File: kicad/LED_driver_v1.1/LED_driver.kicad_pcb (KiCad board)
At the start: 2 copper layers, 34 x 28.2 mm, 7 parts, among them J1 Conn_01x02_Pin, J2 Conn_01x03_Pin

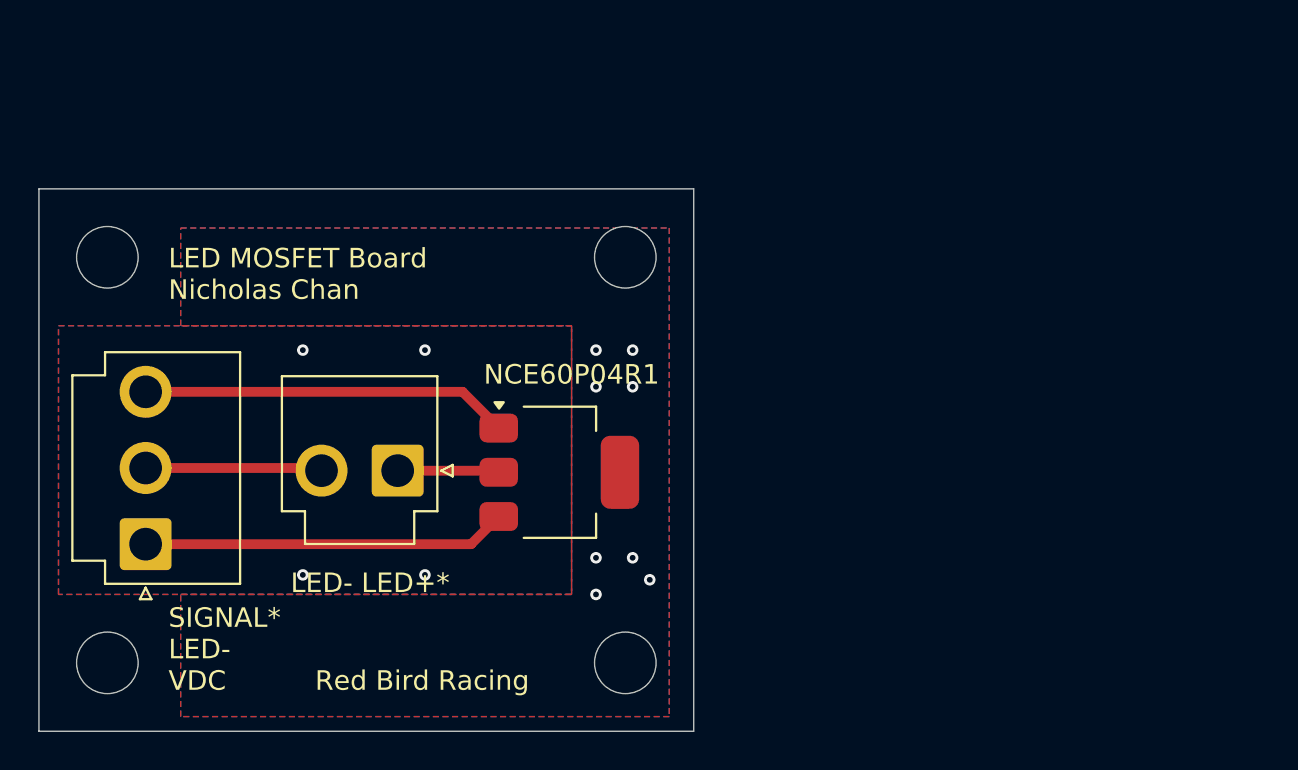
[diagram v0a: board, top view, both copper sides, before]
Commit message: LED drive v2.0
redesigned the mos cus the old one probably doesn't work
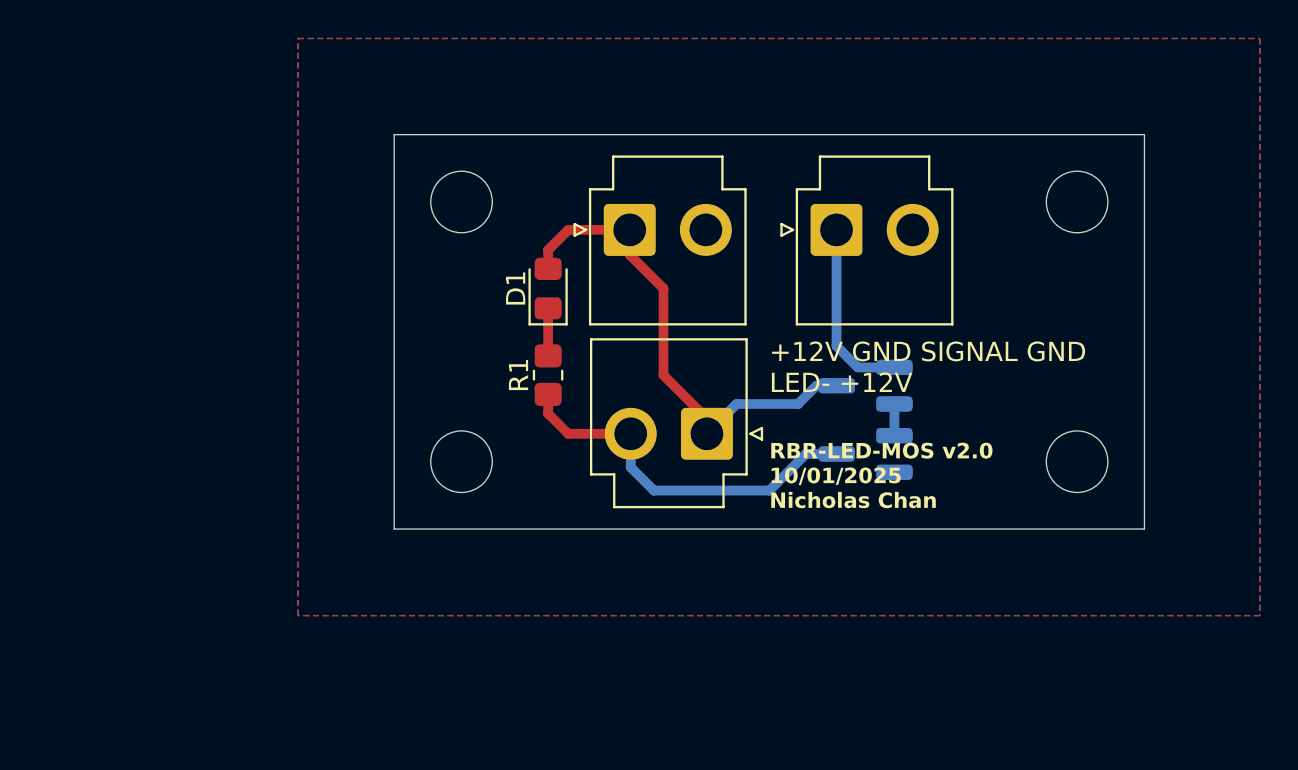
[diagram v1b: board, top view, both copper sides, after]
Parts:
- removed NCE60P04R1: NCE60P04R, Package_TO_SOT_SMD:SOT-223-3_TabPin2
- added D1: LED, LED_SMD:LED_0805_2012Metric_Pad1.15x1.40mm_HandSolder, F.Cu at (108.0, 73.0)
- added J3: Conn_01x02, Connector_JST:JST_VH_B2P-VH_1x02_P3.96mm_Vertical, F.Cu at (116.3, 80.5)
- added Q1: MMBT3904, Package_TO_SOT_SMD:SOT-23_Handsoldering, B.Cu at (124.5, 78.0)
- added Q3: 2N7002, Package_TO_SOT_SMD:SOT-23_Handsoldering, B.Cu at (124.5, 81.6)
- added R1: 1k, Resistor_SMD:R_0805_2012Metric_Pad1.20x1.40mm_HandSolder, F.Cu at (108.0, 77.5)
- J1: value Conn_01x02_Pin -> Conn_01x02
- J2: value Conn_01x03_Pin -> Conn_01x02; footprint Connector_JST:JST_VH_B3P-VH_1x03_P3.96mm_Vertical -> Connector_JST:JST_VH_B2P-VH_1x02_P3.96mm_Vertical
- moved H2 55.8 mm to (135.5, 68.5)
- moved J2 39.5 mm to (123.0, 70.0), turned to 0 degrees
- moved H4 25.7 mm to (135.5, 82.0)
- moved H1 18.6 mm to (103.5, 68.5)
- moved J1 17.4 mm to (112.2, 70.0), turned to 0 degrees
- moved H3 13.6 mm to (103.5, 82.0)
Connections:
- net LED- renamed GND
- J1 pad 1: LED+ -> +12V
- J2 pad 1: VDC -> /SIGNAL
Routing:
- net +12V: track 0.00 -> 25.7 mm
- net /LED-: track 0.00 -> 19.5 mm
- net SIGNAL: track 19.1 -> 0.00 mm
- net VDC: track 19.0 -> 0.00 mm
- net /SIGNAL: track 0.00 -> 9.51 mm
- net GND: track 9.20 -> 0.00 mm, vias 4 -> 0
- net LED+: track 5.29 -> 0.00 mm, vias 8 -> 0
- net Net-(D1-K): track 0.00 -> 2.47 mm
- net Net-(Q1-E): track 0.00 -> 1.65 mm
- removed copper zone on B.Cu, net LED+
- removed copper zone on F.Cu, net LED+
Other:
- board size 34 x 28.2 mm -> 39 x 20.5 mm
- board text added: "+12V GND SIGNAL GND LED- +12V"
- board text added: "RBR-LED-MOS v2.0 10/01/2025 Nicholas Chan"
- board text removed: "LED MOSFET Board Nicholas Chan"
- board text removed: "LED- LED+*"
- board text removed: "Red Bird Racing"
- board text removed: "SIGNAL* LED- VDC"
